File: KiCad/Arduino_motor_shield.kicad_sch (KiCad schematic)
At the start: 16 parts, among them J1 Arduino header 1, J2 DC jack, J3 Arduino header 2, J4 Motors conn, U1 TB6612FNG

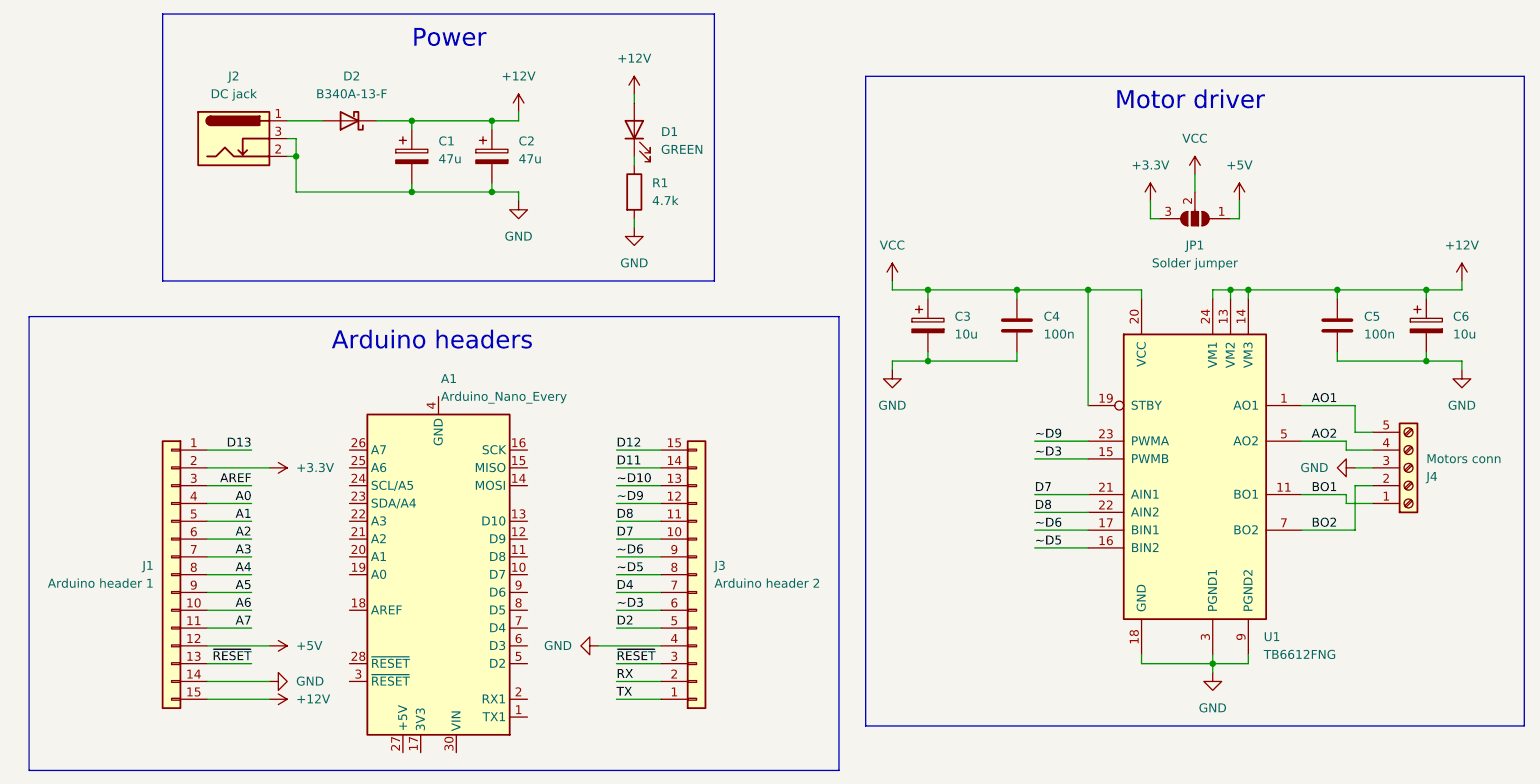
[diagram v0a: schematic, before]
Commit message: Added mounting holes
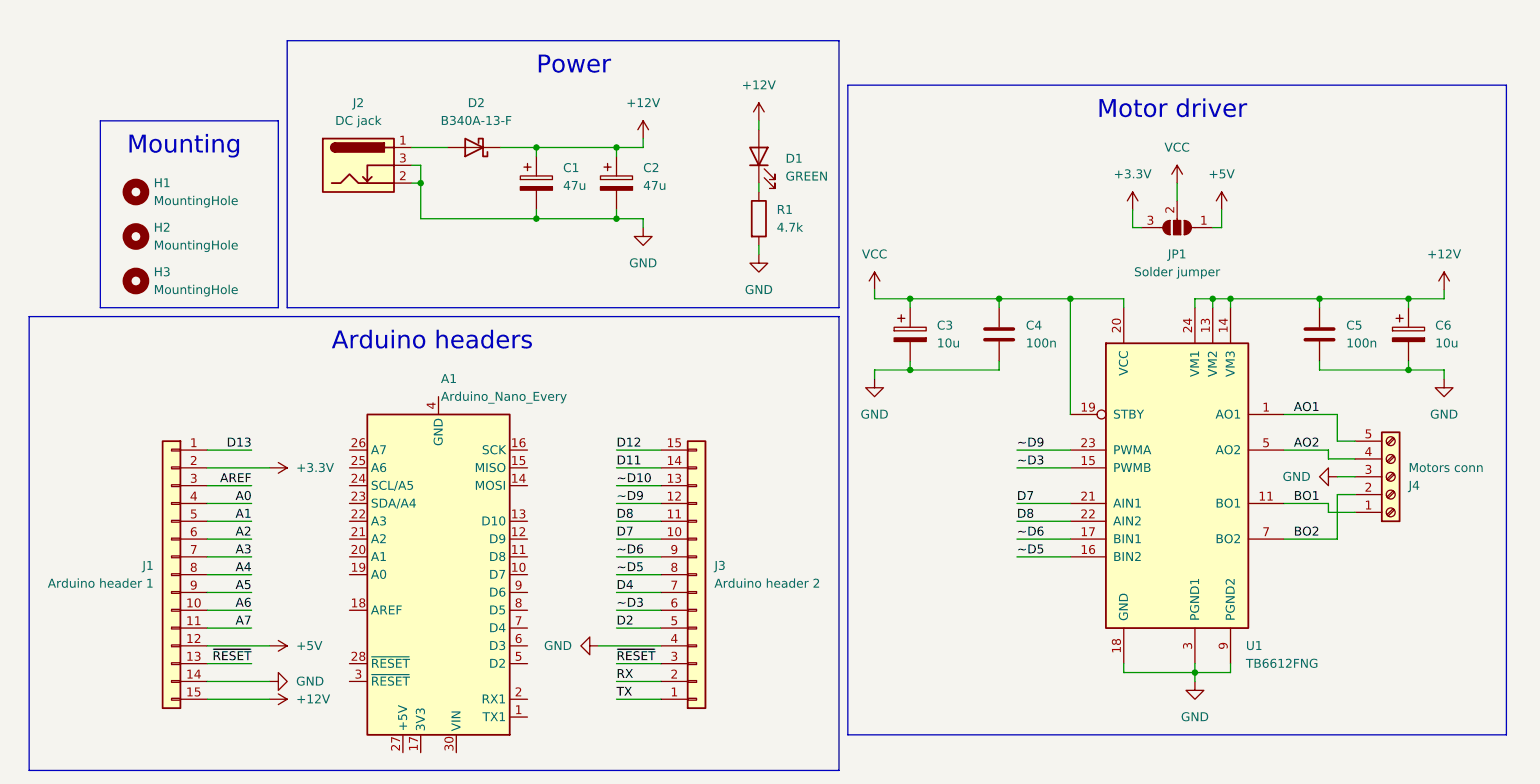
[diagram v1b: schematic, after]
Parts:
- added H1, H2, H3: MountingHole, MountingHole:MountingHole_2.2mm_M2_ISO7380, symbol Mechanical:MountingHole
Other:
- note added: "Mounting"
- moved on the sheet: C1, C2, C3, C4, C5, C6, D1, D2, J2, J4, JP1, R1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

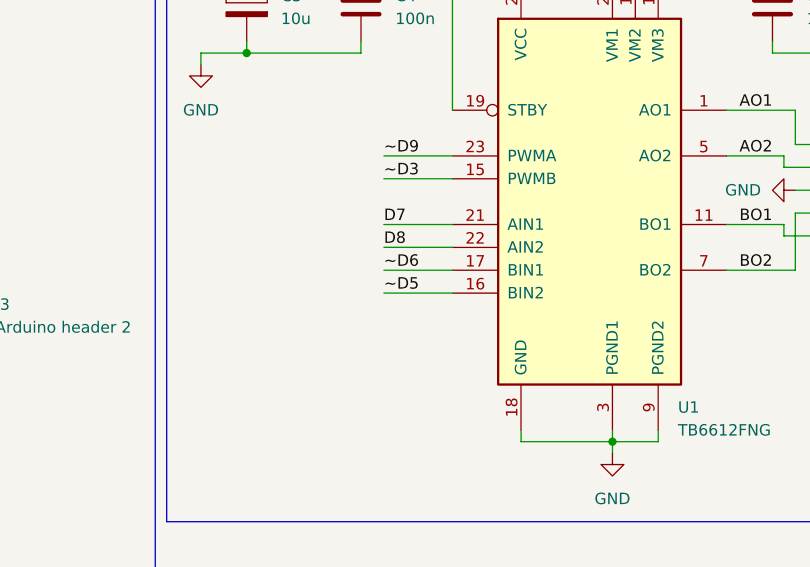
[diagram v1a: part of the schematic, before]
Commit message: Freed up a PWM pin on the Arduino
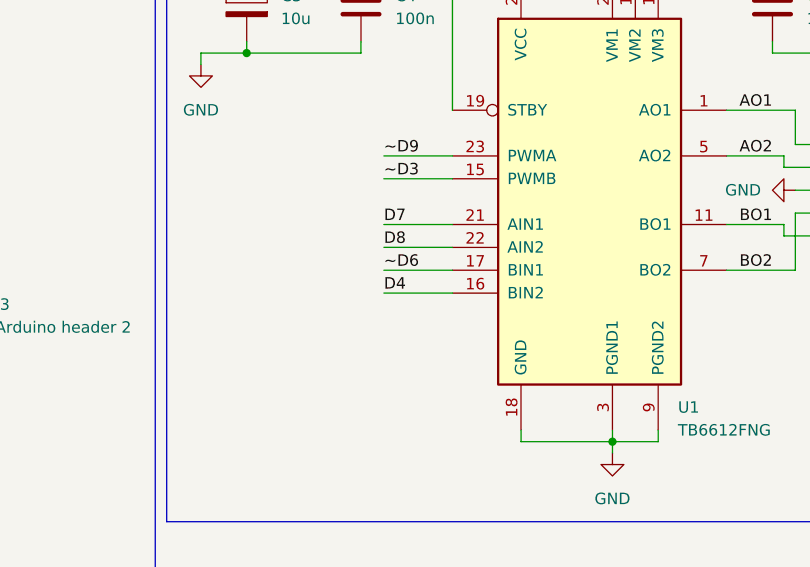
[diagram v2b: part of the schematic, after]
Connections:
- net D4: now also U1.16 (BIN2)
- net ~D5: no longer U1.16 (BIN2)
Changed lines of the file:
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@@
     (effects (font (size 1.27 1.27)) (justify left bottom))
   )
-  (label "~D5" (at 179.07 120.65 0) (fields_autoplaced)
+  (label "D4" (at 179.07 120.65 0) (fields_autoplaced)
     (effects (font (size 1.27 1.27)) (justify left bottom))
   )
